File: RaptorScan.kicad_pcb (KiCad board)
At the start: 2 copper layers, 106 x 72 mm, 14 parts, among them J1 Conn_01x01, J2 Conn_01x01, J3 Conn_01x01, J4 Conn_01x01, J5 Conn_01x01, U1 LM555, U2 NTE4024, U3 NTE4001, U4 NTE4071

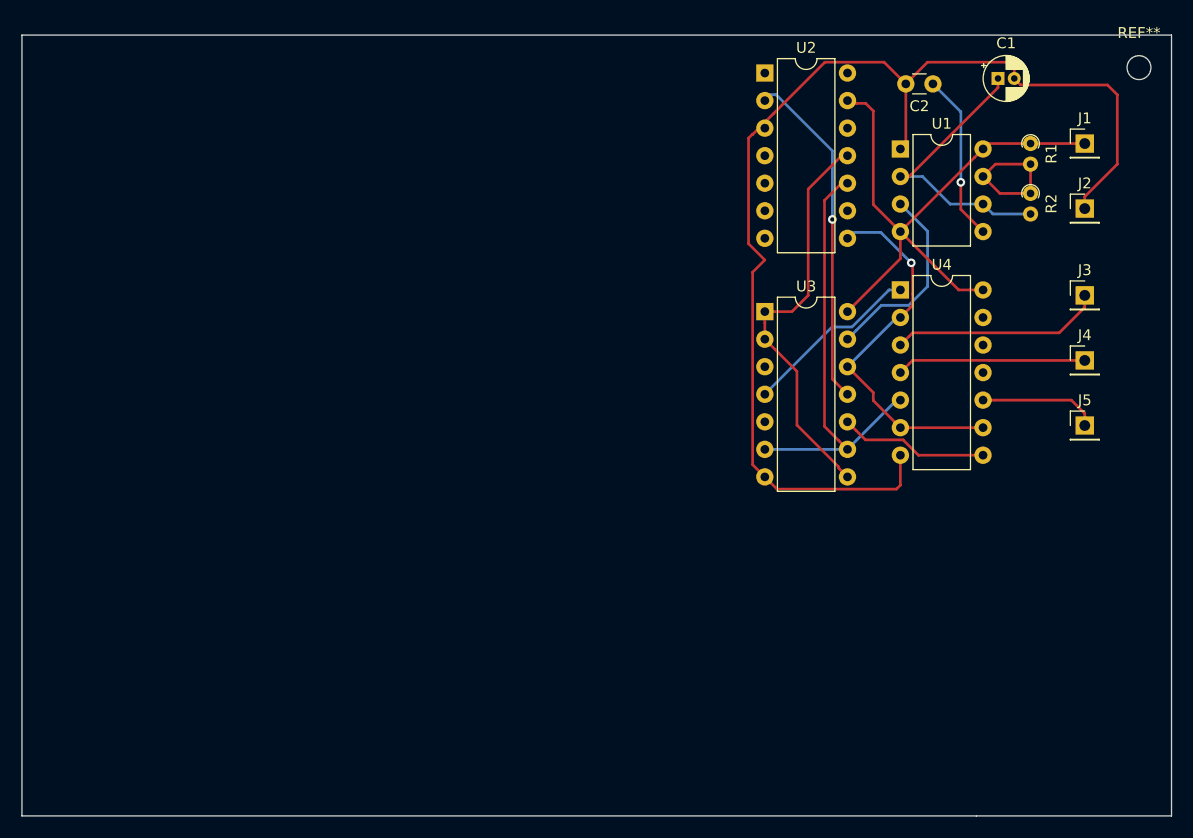
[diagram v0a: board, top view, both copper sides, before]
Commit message: Added: Mounting holes
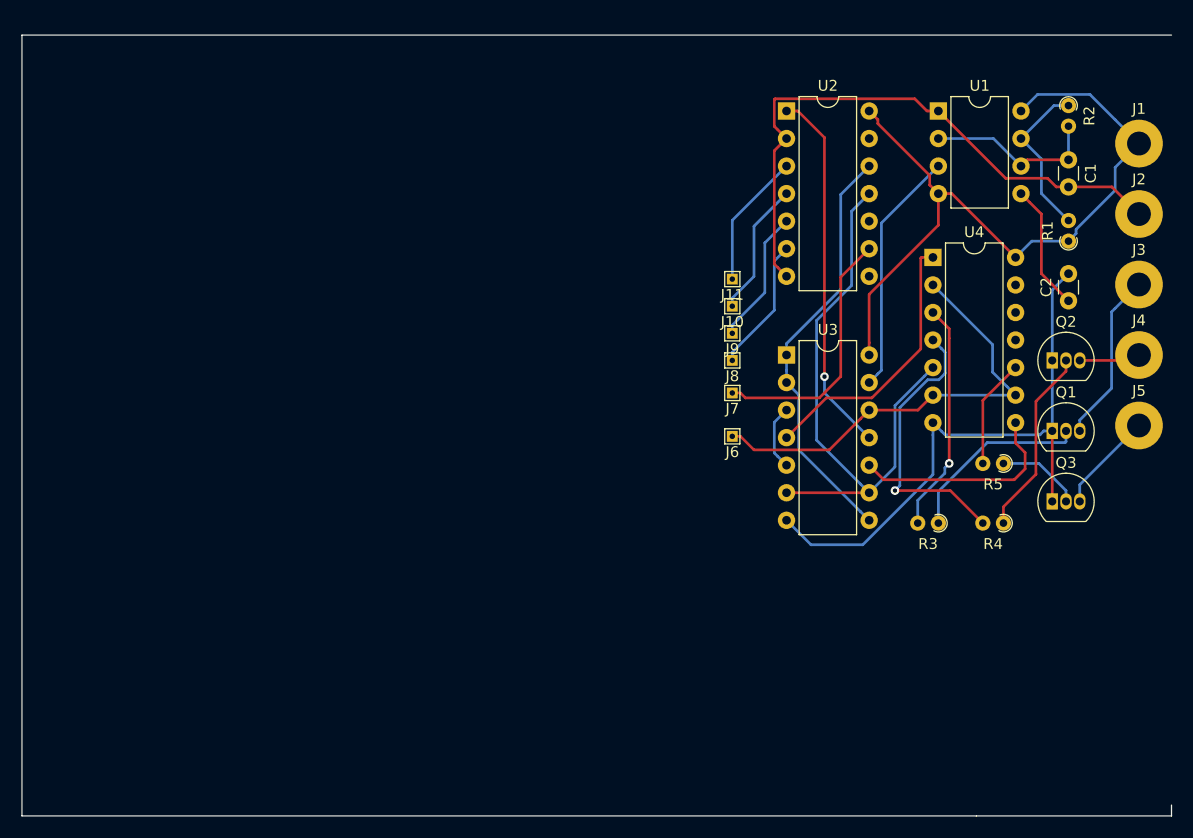
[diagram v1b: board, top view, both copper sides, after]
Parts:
- removed REF**: MountingHole_2.2mm_M2, MountingHole:MountingHole_2.2mm_M2
- added J10: Conn_01x01_Female, TestPoint:TestPoint_THTPad_1.0x1.0mm_Drill0.5mm, F.Cu at (205.5, 84.0)
- added J11: Conn_01x01_Female, TestPoint:TestPoint_THTPad_1.0x1.0mm_Drill0.5mm, F.Cu at (205.5, 81.5)
- added J6: Conn_01x01_Female, TestPoint:TestPoint_THTPad_1.0x1.0mm_Drill0.5mm, F.Cu at (205.5, 96.0)
- added J7: Conn_01x01_Female, TestPoint:TestPoint_THTPad_1.0x1.0mm_Drill0.5mm, F.Cu at (205.5, 92.0)
- added J8: Conn_01x01_Female, TestPoint:TestPoint_THTPad_1.0x1.0mm_Drill0.5mm, F.Cu at (205.5, 89.0)
- added J9: Conn_01x01_Female, TestPoint:TestPoint_THTPad_1.0x1.0mm_Drill0.5mm, F.Cu at (205.5, 86.5)
- added Q1: PN2222A, Package_TO_SOT_THT:TO-92_Inline, F.Cu at (235.0, 95.5)
- added Q2: PN2222A, Package_TO_SOT_THT:TO-92_Inline, F.Cu at (235.0, 89.0)
- added Q3: PN2222A, Package_TO_SOT_THT:TO-92_Inline, F.Cu at (235.0, 102.0)
- added R3: R, Resistor_THT:R_Axial_DIN0204_L3.6mm_D1.6mm_P1.90mm_Vertical, F.Cu at (224.5, 104.0)
- added R4: R, Resistor_THT:R_Axial_DIN0204_L3.6mm_D1.6mm_P1.90mm_Vertical, F.Cu at (230.5, 104.0)
- added R5: R, Resistor_THT:R_Axial_DIN0204_L3.6mm_D1.6mm_P1.90mm_Vertical, F.Cu at (230.5, 98.5)
- C1: footprint Capacitor_THT:CP_Radial_D4.0mm_P1.50mm -> Capacitor_THT:C_Disc_D3.0mm_W1.6mm_P2.50mm
- J1, J2, J3, J4, J5: footprint Connector_PinHeader_2.54mm:PinHeader_1x01_P2.54mm_Vertical -> MountingHole:MountingHole_2.2mm_M2_Pad
- moved C2 23.6 mm to (236.5, 83.5), turned to 90 degrees
- moved C1 9.92 mm to (236.5, 70.5), turned to 270 degrees
- moved R1 9.66 mm to (236.5, 78.0), turned to 90 degrees
- moved R2 8.82 mm to (236.5, 65.5)
- moved J3 5.10 mm to (243.0, 82.0)
- moved J2 5.02 mm to (243.0, 75.5)
- moved J4 5.02 mm to (243.0, 88.5)
- moved J1 5.00 mm to (243.0, 69.0)
- moved J5 5.00 mm to (243.0, 95.0)
- moved U1 4.95 mm to (224.5, 66.0)
- moved U3 4.47 mm to (210.5, 88.5)
- moved U4 4.24 mm to (224.0, 79.5)
- moved U2 4.03 mm to (210.5, 66.0)
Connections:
- J3 pad 1: /MuxDecoder/A -> /LedDriver/Aout
- J4 pad 1: /MuxDecoder/B -> /LedDriver/Bout
- J5 pad 1: /MuxDecoder/C -> /LedDriver/Cout
- U2 pad 3: (no net) -> /7BitCounter/Q6
- U2 pad 4: (no net) -> /7BitCounter/Q5
- U2 pad 5: (no net) -> /7BitCounter/Q4
- U2 pad 6: (no net) -> /7BitCounter/Q3
- U3 pad 12: /7BitCounter/Q2 -> /MuxDecoder/Z
- U4 pad 2: /7BitCounter/Q2 -> /MuxDecoder/Z
- U4 pad 6: /7BitCounter/Q2 -> /MuxDecoder/Z
- U4 pad 9: /7BitCounter/Q2 -> /MuxDecoder/Z
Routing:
- net /MuxDecoder/Z: track 0.00 -> 42.0 mm
- net Net-(Q1-Pad2): track 0.00 -> 17.6 mm
- net Net-(Q2-Pad2): track 0.00 -> 17.4 mm
- net /LedDriver/Aout: track 0.00 -> 15.8 mm
- net +12V: track 54.8 -> 67.9 mm
- net /7BitCounter/Q6: track 0.00 -> 12.5 mm
- net /7BitCounter/Q5: track 0.00 -> 12.5 mm
- net /7BitCounter/Q4: track 0.00 -> 12.4 mm
- net /7BitCounter/Q3: track 0.00 -> 12.4 mm
- net /7BitCounter/Q1: track 41.2 -> 53.2 mm
- net /7BitCounter/Q2: track 34.6 -> 23.9 mm, vias 1 -> 0
- net Net-(C1-Pad1): track 26.7 -> 16.4 mm
- net /LedDriver/Cout: track 0.00 -> 9.26 mm
- net Net-(U3-Pad4): track 16.5 -> 25.3 mm
- net /MuxDecoder/B: track 17.5 -> 26.2 mm, vias 0 -> 1
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
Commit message: Update: BOM
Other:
- board size 106 x 72 mm -> 44.5 x 45.3 mm
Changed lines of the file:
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@@
     )
   )
-  (gr_line (start 246 131) (end 228 131) (layer Edge.Cuts) (width 0.05))
-  (gr_line (start 246 130) (end 246 131) (layer Edge.Cuts) (width 0.05))
-  (gr_line (start 140 59) (end 246 59) (layer Edge.Cuts) (width 0.05))
-  (gr_line (start 140 131) (end 140 59) (layer Edge.Cuts) (width 0.05))
-  (gr_line (start 228 131) (end 140 131) (layer Edge.Cuts) (width 0.05))
+  (gr_line (start 201.3 61.2) (end 217.9 61.2) (layer Edge.Cuts) (width 0.05))
+  (gr_line (start 201.3 106.5) (end 201.3 61.2) (layer Edge.Cuts) (width 0.05))
+  (gr_line (start 245.8 106.5) (end 201.3 106.5) (layer Edge.Cuts) (width 0.05))
+  (gr_line (start 245.8 61.2) (end 245.8 106.5) (layer Edge.Cuts) (width 0.05))
+  (gr_line (start 203.4 61.2) (end 245.8 61.2) (layer Edge.Cuts) (width 0.05))
   (segment (start 224.799999 95.539999) (end 224 94.74) (width 0.25) (layer B.Cu) (net 1))
   (segment (start 225.125001 95.865001) (end 224.799999 95.539999) (width 0.25) (layer B.Cu) (net 1))
